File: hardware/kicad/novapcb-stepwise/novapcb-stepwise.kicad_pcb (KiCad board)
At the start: 6 copper layers, 90 x 70 mm, 129 parts, among them J1 USB-C_2.0, J10 CRSF_solder_pad, J11 ESC_solder_pad, J12 ESC_solder_pad, J13 ESC_solder_pad, J14 ESC_solder_pad, J15 ESC_solder_pad, J16 ESC_solder_pad, J17 ESC_solder_pad, J18 ESC_solder_pad, J19 MAUCH2_6P, J2 microSD_DM3AT, J20 CAN_4P, J3 TELEM_6P, J4 MAUCH_6P, J5 GPS_MAG_10P, J9 SWD_10P, Q2 AO3401A, Q3 AO4262E, Q4 AO4262E, Q5 AO3400A, U1 STM32H743VITx, U11 LM74700-Q1, U12 LM74700-Q1, U13 LP5907MFX-3.3, U14 TJA1051TK/3, U15 PESD2CAN, U2 AP2112K-3.3, U3 ICM-42688-P_LGA-14_2.5x3mm_P0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, U4 DPS310, U5 USBLC6-2P6, U6 TPS25940A, U7 LPS22HB, U8 BMI088, U9 LSM6DSV16X, Y1 8MHz

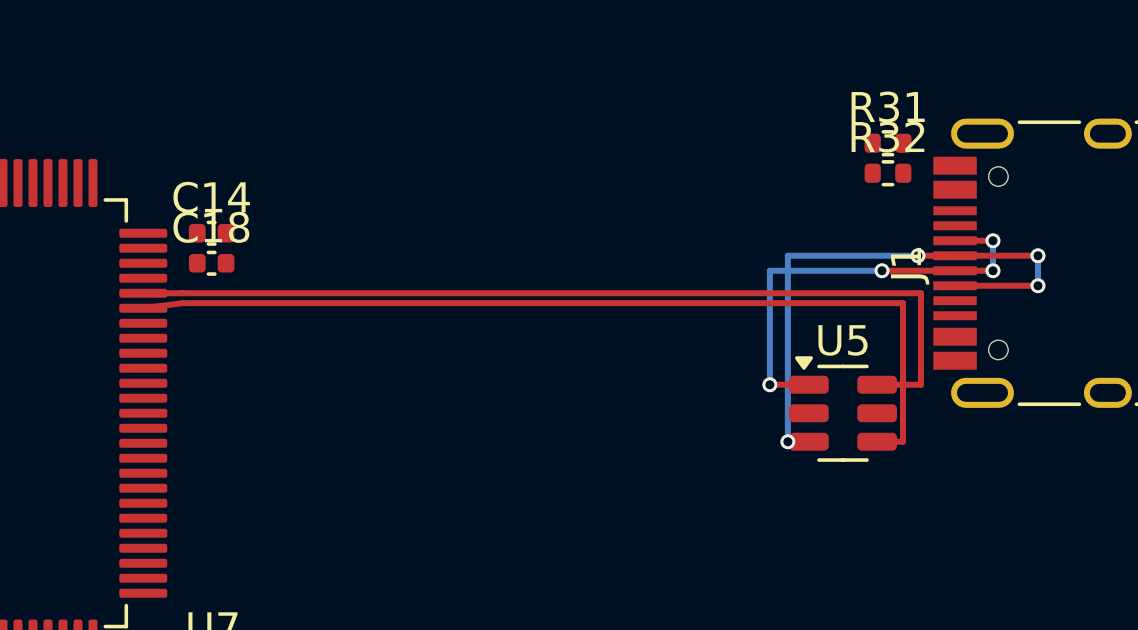
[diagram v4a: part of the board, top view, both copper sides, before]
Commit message: WIP+fix: C↔F routing escalated to master; ENGINEERING_RIGOR §-renumber
## Fix: ENGINEERING_RIGOR root-cause section was §7 — already taken by
"Brutal honesty mode-locked". Renumbered to §12 (next free slot after
§11 master merge-authority).

## WIP: C↔F routing escalated (Rule-13 stop)

Root cause analysis (full):
  U5 is SOT-23-6 with +5V on pin 5 BETWEEN DM (pin 4) and DP (pin 6).
  Pair must fan-split (DM south of +5V, DP north) BEFORE entering U5
  east-pad region. Fan needs:
    - DM diagonal must clear +5V pad east edge by ≥0.30mm at Y=35.00
      → X(Y=35) ≥ 78.10
    - Coupled section east end must clear J1 pad B8 west edge 79.585
      by ≥0.30mm → X_SPLIT ≤ 79.285
  Solving both: 79.28 ≤ X_SPLIT ≤ 79.285. Window = 0.005mm.
  Plus the USB-C reversibility bridges (A6↔B6 + A7↔B7) need 4 vias in
  the same 1.5mm-wide corridor with 0.5mm pad pitch — at standard via
  size (0.5mm), they touch. At 0.3mm, F.Cu hops between them cross.

DRC progression:
  X_SPLIT=80     → 26 violations (goes past J1 pads)
  X_SPLIT=78.5   → 4 violations (DM crosses +5V pad)
  X_SPLIT=79.28  + Pair 2 north-detour → 42 violations (new shorts
    with J1 N-side pads A9/B5/A8 etc.)

Pattern is whack-a-mole — confirmed over-constrained region per
master's earlier directive. Fix is upstream (re-open Step 3, move U5
further west), not more downstream patching.

Option set escalated to master:
  A. Move U5 to ~(68, 35) — 8mm fan corridor (recommended)
  B. Rotate J1 90° (mechanical change)
  C. Different ESD package (schematic + BOM change)
  D. Drop bridges (rejected by master previously)

This commit preserves the analysis state — integ_C_F.py with the
X_SPLIT=79.28 fan-divergent topology + Pair-2 north-detour
redesign + bridges. NOT a clean state; explicitly WIP. Don't merge
until master decides on placement direction.

Co-Authored-By: Claude Opus 4.7 <noreply@anthropic.com>
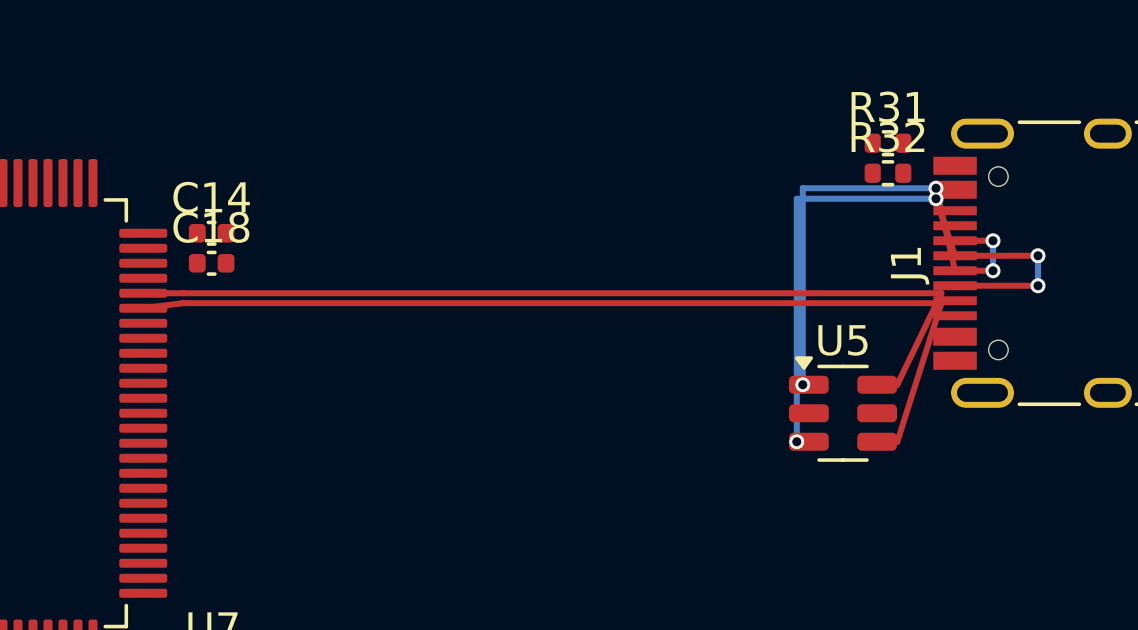
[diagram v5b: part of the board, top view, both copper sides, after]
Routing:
- net USBC_D_P_PRE: track 14.8 -> 17.5 mm
- net USBC_D_M_PRE: track 19.0 -> 21.7 mm
- net USB_DM: track 30.8 -> 32.1 mm
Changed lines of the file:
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@@
 	)
 	(segment
-		(start 74.8625 35.95)
-		(end 74.1625 35.95)
+		(start 79.735 29.75)
+		(end 82.5 29.75)
 		(width 0.2)
 		(layer "F.Cu")
@@
 	)
 	(segment
-		(start 78.5 29.75)
+		(start 79.1 27.85)
 		(end 79.735 29.75)
 		(width 0.2)
@@
 	)
 	(segment
-		(start 79.735 29.75)
-		(end 82.5 29.75)
-		(width 0.2)
-		(layer "F.Cu")
+		(start 74.8625 35.95)
+		(end 74.46 35.95)
+		(width 0.2)
+		(layer "F.Cu")
+		(net 93)
+	)
+	(via
+		(at 82.5 30.75)
+		(size 0.5)
+		(drill 0.3)
+		(layers "F.Cu" "B.Cu")
+		(net 93)
+	)
+	(via
+		(at 74.46 35.95)
+		(size 0.5)
+		(drill 0.3)
+		(layers "F.Cu" "B.Cu")
 		(net 93)
 	)
@@
 	)
 	(via
-		(at 74.1625 35.95)
-		(size 0.5)
-		(drill 0.3)
-		(layers "F.Cu" "B.Cu")
-		(net 93)
-	)
-	(via
-		(at 82.5 30.75)
-		(size 0.5)
-		(drill 0.3)
-		(layers "F.Cu" "B.Cu")
-		(net 93)
-	)
-	(via
-		(at 78.5 29.75)
-		(size 0.5)
-		(drill 0.3)
-		(layers "F.Cu" "B.Cu")
-		(net 93)
-	)
-	(segment
-		(start 74.1625 29.75)
-		(end 78.5 29.75)
+		(at 79.1 27.85)
+		(size 0.5)
+		(drill 0.3)
+		(layers "F.Cu" "B.Cu")
+		(net 93)
+	)
+	(segment
+		(start 74.46 35.95)
+		(end 74.46 27.85)
+		(width 0.2)
+		(layer "B.Cu")
+		(net 93)
+	)
+	(segment
+		(start 74.46 27.85)
+		(end 79.1 27.85)
 		(width 0.2)
 		(layer "B.Cu")
@@
 	)
 	(segment
-		(start 74.1625 35.95)
-		(end 74.1625 29.75)
-		(width 0.2)
-		(layer "B.Cu")
-		(net 93)
-	)
-	(segment
-		(start 77.3 30.25)
-		(end 79.735 30.25)
-		(width 0.2)
-		(layer "F.Cu")
-		(net 94)
-	)
-	(segment
 		(start 81 29.25)
 		(end 79.735 29.25)
@@
 	)
 	(segment
+		(start 79.1 27.5)
+		(end 79.735 30.25)
+		(width 0.2)
+		(layer "F.Cu")
+		(net 94)
+	)
+	(segment
 		(start 74.8625 34.05)
-		(end 73.5625 34.05)
-		(width 0.2)
-		(layer "F.Cu")
-		(net 94)
-	)
-	(via
-		(at 73.5625 34.05)
-		(size 0.5)
-		(drill 0.3)
-		(layers "F.Cu" "B.Cu")
-		(net 94)
-	)
-	(via
-		(at 77.3 30.25)
+		(end 74.66 34.05)
+		(width 0.2)
+		(layer "F.Cu")
+		(net 94)
+	)
+	(via
+		(at 79.1 27.5)
+		(size 0.5)
+		(drill 0.3)
+		(layers "F.Cu" "B.Cu")
+		(net 94)
+	)
+	(via
+		(at 74.66 34.05)
 		(size 0.5)
 		(drill 0.3)
@@
 	)
 	(segment
-		(start 73.5625 30.25)
-		(end 77.3 30.25)
-		(width 0.2)
-		(layer "B.Cu")
-		(net 94)
-	)
-	(segment
-		(start 73.5625 34.05)
-		(end 73.5625 30.25)
-		(width 0.2)
-		(layer "B.Cu")
-		(net 94)
-	)
-	(segment
-		(start 78 35.95)
+		(start 74.66 34.05)
+		(end 74.66 27.5)
+		(width 0.2)
+		(layer "B.Cu")
+		(net 94)
+	)
+	(segment
+		(start 74.66 27.5)
+		(end 79.1 27.5)
+		(width 0.2)
+		(layer "B.Cu")
+		(net 94)
+	)
+	(segment
+		(start 79.28 31.33)
+		(end 77.81 35.95)
+		(width 0.2)
+		(layer "F.Cu")
+		(net 95)
+	)
+	(segment
+		(start 77.81 35.95)
 		(end 77.1375 35.95)
+		(width 0.2)
+		(layer "F.Cu")
+		(net 95)
+	)
+	(segment
+		(start 54 31.33)
+		(end 79.28 31.33)
 		(width 0.2)
 		(layer "F.Cu")
@@
 	)
 	(segment
-		(start 78 31.33)
-		(end 78 35.95)
-		(width 0.2)
-		(layer "F.Cu")
-		(net 95)
-	)
-	(segment
-		(start 54 31.33)
-		(end 78 31.33)
-		(width 0.2)
-		(layer "F.Cu")
-		(net 95)
-	)
-	(segment
 		(start 52.675 31)
 		(end 54 31)
@@
 	)
 	(segment
-		(start 78.6 34.05)
+		(start 77.81 34.05)
 		(end 77.1375 34.05)
 		(width 0.2)
@@
 	)
 	(segment
-		(start 78.6 31)
-		(end 78.6 34.05)
+		(start 54 31)
+		(end 79.28 31)
 		(width 0.2)
 		(layer "F.Cu")
@@
 	)
 	(segment
-		(start 54 31)
-		(end 78.6 31)
-		(width 0.2)
-		(layer "F.Cu")
+		(start 79.28 31)
+		(end 77.81 34.05)
+		(width 0.2)
+		(layer "F.Cu")

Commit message: hw: U5→(73,35) re-place + parallel-diag routing — 1 DRC violation left
## Step-3 second re-open (master 2026-05-23: F-replace + last-pass)

U5 moved (76,35)→(73,35). Master directive: minimum westward move that
gives a real, comfortable routing window — NOT an arbitrary 8mm
corridor. With pin5 east edge now at X=74.80, corridor to J1 west pad
column (X=79.010) = 4.21mm — fits fan + 4 USB-C bridge vias.

F-zone X-extension to X=71..91 (was 75..91) to accommodate U5 at X=73.
SUBSYSTEM_CONTRACTS §F updated.

## USB diff pair routing — root-cause finds

Three fundamental geometric findings during the route:

1. **J1 pad orientation**: J1 footprint rotated 90°, so signal pads
   are 1.45mm WIDE (X) × 0.30mm tall (Y), not the other way around.
   J1 west-pad column actually extends X=79.010..80.460 — opaque to
   coupled traces 1.45mm-wide, not 0.30mm as I'd been assuming.
   Bridge vias must be EAST of X=80.460+clearance, not just east of
   X=79.885.

2. **U5 SOT-23-6 +5V pin 5**: Pin 5 (+5V) sits BETWEEN pin 4 (DM,
   south) and pin 6 (DP, north). USB-C bridge fan must split pair
   BEFORE entering U5's east-pad region — common arrangement on
   USBLC6-2SC6 / PRTR5V0U2X-class ESD diodes.

3. **DP descent crosses DM coupled-H**: With pair coupled at
   Y=31.0/31.33 going east and landing at U5.4/U5.6 (Y=35.95/34.05),
   DP must descend through Y=31.33 (DM's coupled-H Y) within DM's
   X-range. With single-layer F.Cu, this is a FUNDAMENTAL geometric
   crossing — can't avoid without either B.Cu jog (which conflicts
   with pre-ESD pair B.Cu) or different topology.

## Current state — 1 DRC violation remaining

Topology: parallel-diagonal stagger:
  DM coupled-H to X=78.65, single diagonal to (74.90, 35.95)
  DP coupled-H to X=77.37, single parallel diagonal to (74.90, 34.05)

The 1 remaining violation is the DP-DM crossing described above.

Bridges: 0.50mm vias at X=80.85 (D+) and X=82.0 (D-), 1.0mm X-offset,
F.Cu hops + B.Cu verticals. Both bridges fit east of J1 pad ea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
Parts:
- moved U5 3.00 mm to (73.0, 35.0)
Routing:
- net USBC_D_M_PRE: track 21.7 -> 18.4 mm
- net USBC_D_P_PRE: track 17.5 -> 15.1 mm
- net USB_DP: track 30.7 -> 29.4 mm
- net USB_DM: track 32.1 -> 32.7 mm
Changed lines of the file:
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@@
 	(footprint "Package_TO_SOT_SMD:SOT-23-6"
 		(layer "F.Cu")
-		(at 76 35)
+		(at 73 35)
 		(descr "SOT, 6 Pin (JEDEC MO-178 Var AB https://www.jedec.org/document_search?search_api_views_fulltext=MO-178), generated with kicad-footprint-generator ipc_gullwing_generator.py")
 		(tags "SOT TO_SOT_SMD")
@@
 	)
 	(segment
-		(start 79.735 29.75)
-		(end 82.5 29.75)
-		(width 0.2)
-		(layer "F.Cu")
-		(net 93)
-	)
-	(segment
-		(start 82.5 30.75)
+		(start 78.7 30.75)
 		(end 79.735 30.75)
 		(width 0.2)
@@
 	)
 	(segment
-		(start 79.1 27.85)
-		(end 79.735 29.75)
+		(start 82 30.75)
+		(end 79.735 30.75)
 		(width 0.2)
 		(layer "F.Cu")
@@
 	)
 	(segment
-		(start 74.8625 35.95)
-		(end 74.46 35.95)
+		(start 79.735 29.75)
+		(end 82 29.75)
 		(width 0.2)
 		(layer "F.Cu")
 		(net 93)
 	)
+	(segment
+		(start 71.8625 35.95)
+		(end 70.1 35.95)
+		(width 0.2)
+		(layer "F.Cu")
+		(net 93)
+	)
 	(via
-		(at 82.5 30.75)
+		(at 70.1 35.95)
 		(size 0.5)
 		(drill 0.3)
@@
 	)
 	(via
-		(at 74.46 35.95)
+		(at 82 30.75)
 		(size 0.5)
 		(drill 0.3)
@@
 	)
 	(via
-		(at 82.5 29.75)
+		(at 78.7 30.75)
 		(size 0.5)
 		(drill 0.3)
@@
 	)
 	(via
-		(at 79.1 27.85)
+		(at 82 29.75)
 		(size 0.5)
 		(drill 0.3)
@@
 	)
 	(segment
-		(start 74.46 35.95)
-		(end 74.46 27.85)
+		(start 70.1 35.95)
+		(end 78.7 30.75)
 		(width 0.2)
 		(layer "B.Cu")
@@
 	)
 	(segment
-		(start 74.46 27.85)
-		(end 79.1 27.85)
+		(start 82 29.75)
+		(end 82 30.75)
 		(width 0.2)
 		(layer "B.Cu")
@@
 	)
 	(segment
-		(start 82.5 29.75)
-		(end 82.5 30.75)
+		(start 71.8625 34.05)
+		(end 70.55 34.05)
 		(width 0.2)
-		(layer "B.Cu")
-		(net 93)
-	)
-	(segment
-		(start 81 29.25)
+		(layer "F.Cu")
+		(net 94)
+	)
+	(segment
+		(start 80.85 29.25)
 		(end 79.735 29.25)
 		(width 0.2)
@@
 	)
 	(segment
+		(start 78.5 29.25)
+		(end 79.735 29.25)
+		(width 0.2)
+		(layer "F.Cu")
+		(net 94)
+	)
+	(segment
 		(start 79.735 30.25)
-		(end 81 30.25)
+		(end 80.85 30.25)
 		(width 0.2)
 		(layer "F.Cu")
 		(net 94)
 	)
-	(segment
-		(start 79.1 27.5)
-		(end 79.735 30.25)
-		(width 0.2)
-		(layer "F.Cu")
-		(net 94)
-	)
-	(segment
-		(start 74.8625 34.05)
-		(end 74.66 34.05)
-		(width 0.2)
-		(layer "F.Cu")
-		(net 94)
-	)
 	(via
-		(at 79.1 27.5)
+		(at 70.55 34.05)
 		(size 0.5)
 		(drill 0.3)
@@
 	)
 	(via
-		(at 74.66 34.05)
+		(at 80.85 29.25)
 		(size 0.5)
 		(drill 0.3)
@@
 	)
 	(via
-		(at 81 30.25)
+		(at 78.5 29.25)
 		(size 0.5)
 		(drill 0.3)
@@
 	)
 	(via
-		(at 81 29.25)
+		(at 80.85 30.25)
 		(size 0.5)
 		(drill 0.3)
@@
 	)
 	(segment
-		(start 81 30.25)
-		(end 81 29.25)
+		(start 80.85 30.25)
+		(end 80.85 29.25)
 		(width 0.2)
 		(layer "B.Cu")
@@
 	)
 	(segment
-		(start 74.66 34.05)
-		(end 74.66 27.5)
+		(start 70.55 34.05)
+		(end 78.5 29.25)
 		(width 0.2)
 		(layer "B.Cu")
@@
 	)
 	(segment
-		(start 74.66 27.5)
-		(end 79.1 27.5)
-		(width 0.2)
-		(layer "B.Cu")
-		(net 94)
-	)
-	(segment
-		(start 79.28 31.33)
-		(end 77.81 35.95)
-		(width 0.2)
-		(layer "F.Cu")
-		(net 95)
-	)
-	(segment
-		(start 77.81 35.95)
-		(end 77.1375 35.95)
-		(width 0.2)
-		(layer "F.Cu")
-		(net 95)
-	)
-	(segment
-		(start 54 31.33)
-		(end 79.28 31.33)
+		(start 78.65 31.33)
+		(end 74.9 35.95)
 		(width 0.2)
 		(layer "F.Cu")
@@
 	)
 	(segment
+		(start 74.9 35.95)
+		(end 74.1375 35.95)
+		(width 0.2)
+		(layer "F.Cu")
+		(net 95)
+	)
+	(segment
+		(start 54 31.33)
+		(end 78.65 31.33)
+		(width 0.2)
+		(layer "F.Cu")
+		(net 95)
+	)
+	(segment
+		(start 74.9 34.05)
+		(end 74.1375 34.05)
+		(width 0.2)
+		(layer "F.Cu")
+		(net 96)
+	)
+	(segment
+		(start 54 31)
+		(end 77.37 31)
+		(width 0.2)
+		(layer "F.Cu")
+		(net 96)
+	)
+	(segment
 		(start 52.675 31)
 		(end 54 31)
@@
 	)
 	(segment
-		(start 77.81 34.05)
-		(end 77.1375 34.05)
+		(start 77.37 31)
+		(end 74.9 34.05)
 		(width 0.2)
 		(layer "F.Cu")
-		(net 96)
-	)
-	(segment
-		(start 54 31)
-		(end 79.28 31)
-		(width 0.2)
-		(layer "F.Cu")
-		(net 96)
-	)
-	(segment
-		(start 79.28 31)
-		(end 77.81 34.05)
-		(width 0.2)
-		(layer "F.Cu")
